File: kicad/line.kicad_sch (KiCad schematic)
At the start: 58 parts, among them J3 AudioJack3_Switch, J4 AudioJack3_Switch, Q2 CSD13380F3, Q3 CSD13380F3, SW12 RotaryEncoder, U12 OPA1637, U13 OPA1637

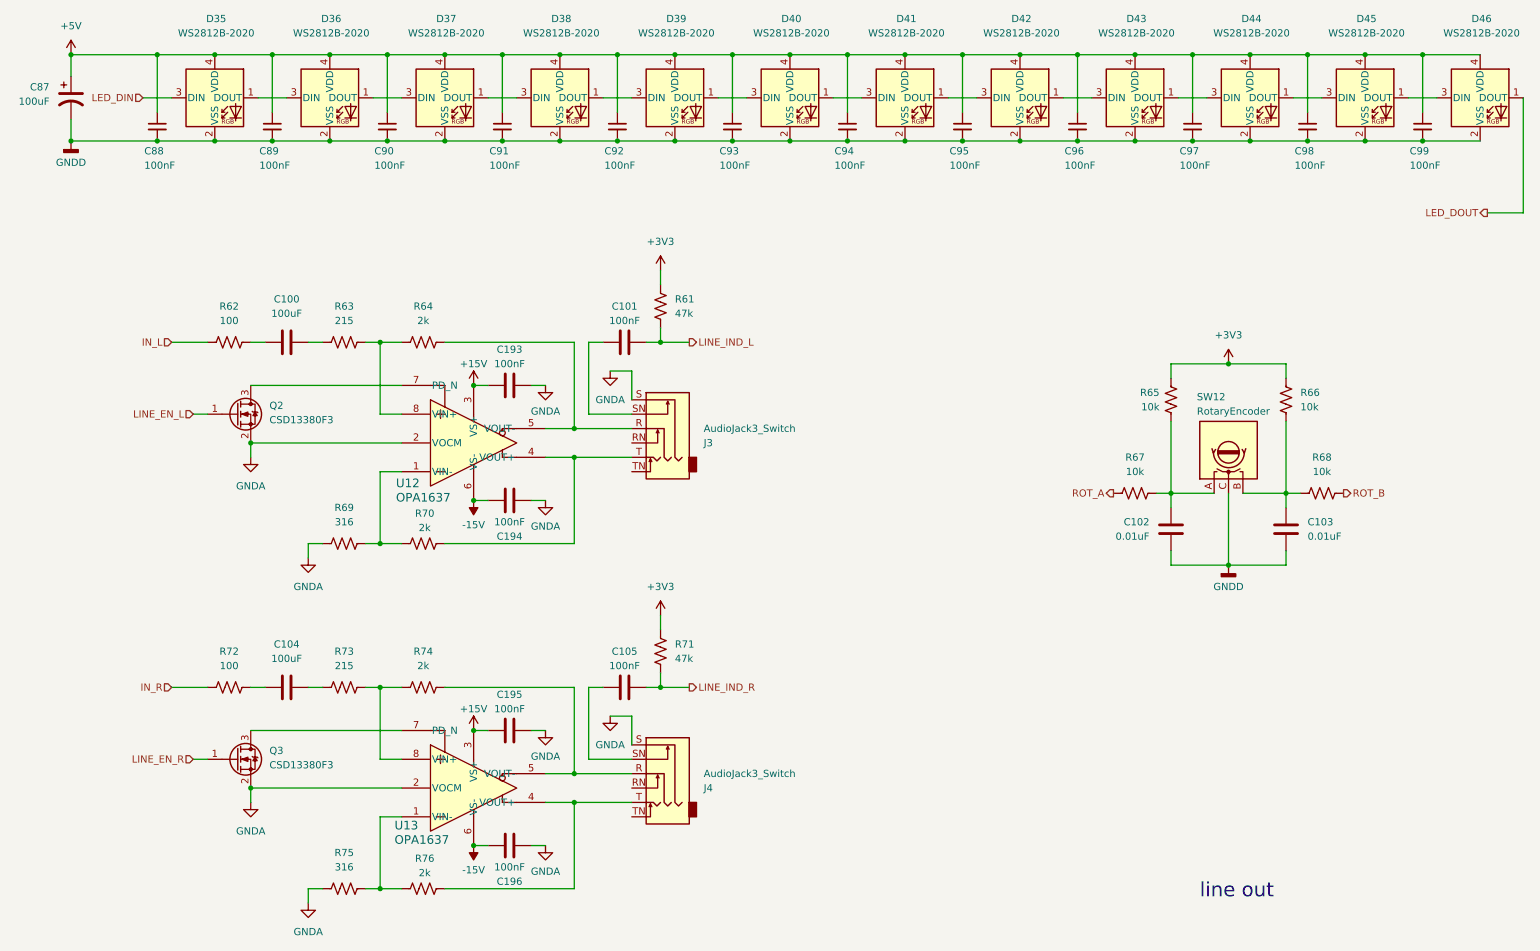
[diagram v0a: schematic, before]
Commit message: output stage impedances
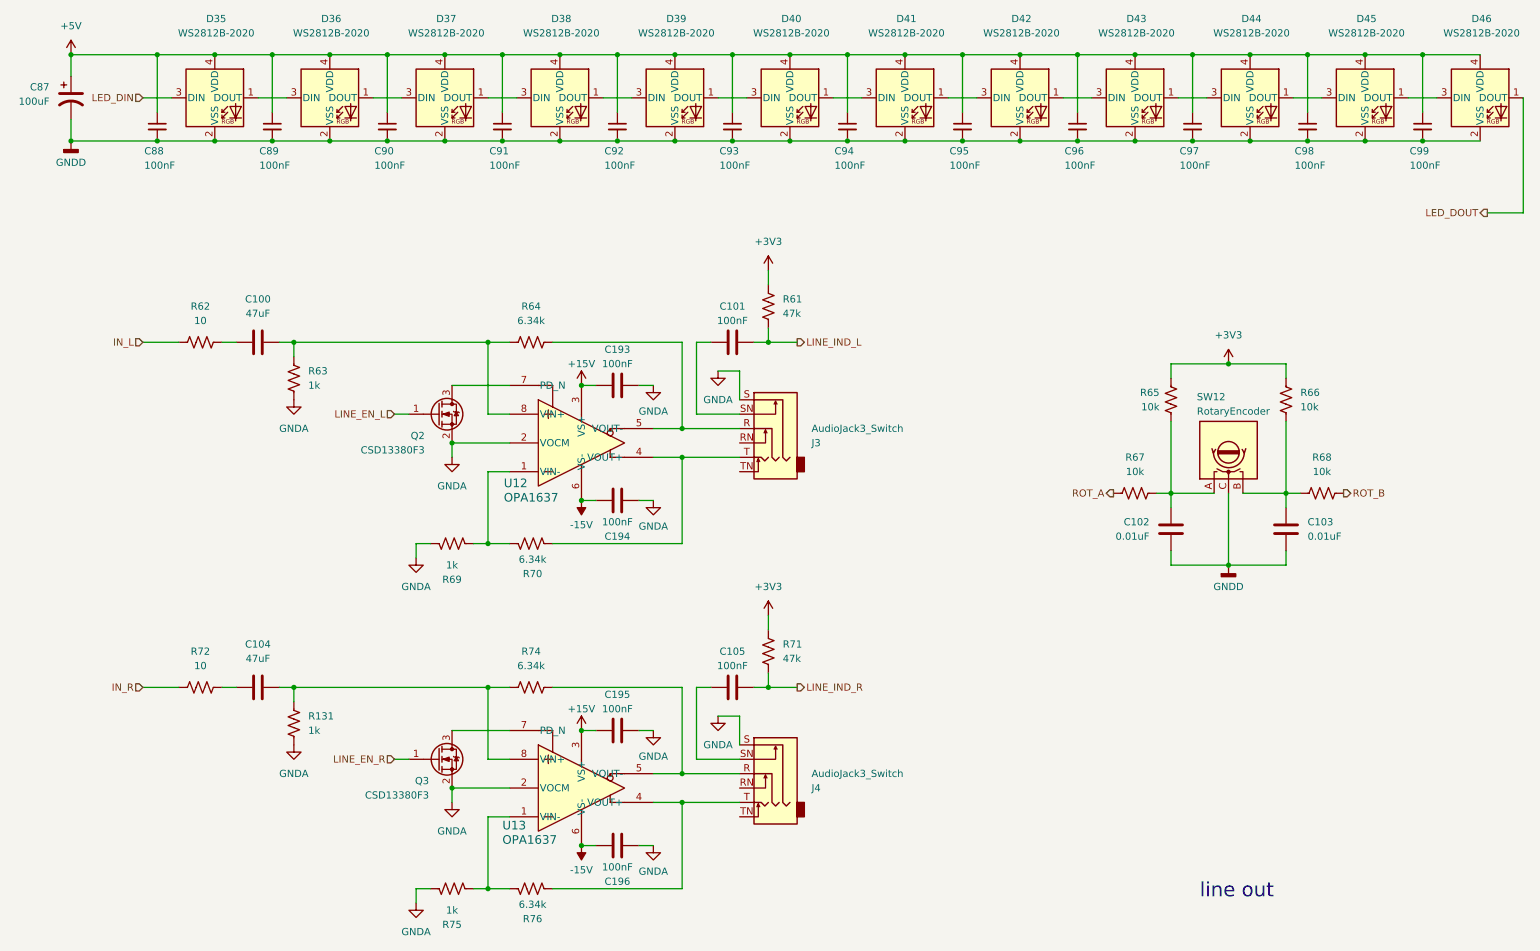
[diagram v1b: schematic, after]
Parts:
- removed R73: 215, symbol Device:R_US
- added R131: 1k, symbol Device:R_US
- C100, C104: value 100uF -> 47uF
- R62, R72: value 100 -> 10
- R63: value 215 -> 1k
- R64, R70, R74, R76: value 2k -> 6.34k
- R69, R75: value 316 -> 1k
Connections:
- net GNDA: now also R63.1, R131.1
- net at R74.1, U13.8 (VIN+): now also C104.2, R131.2
- net at R63.2, R64.1, U12.8 (VIN+): now also C100.2
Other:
- moved on the sheet: C100, C101, C104, C105, C193, C194, C195, C196, J3, J4, Q2, Q3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

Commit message: #16
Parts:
- C102, C103: value 0.01uF -> 10nF
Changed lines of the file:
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@@
 			)
 		)
-		(property "Value" "0.01uF"
+		(property "Value" "10nF"
 			(at 215.9 111.7599 0)
 			(show_name no)
@@
 			)
 		)
-		(property "Value" "0.01uF"
+		(property "Value" "10nF"
 			(at 243.84 111.7599 0)
 			(show_name no)

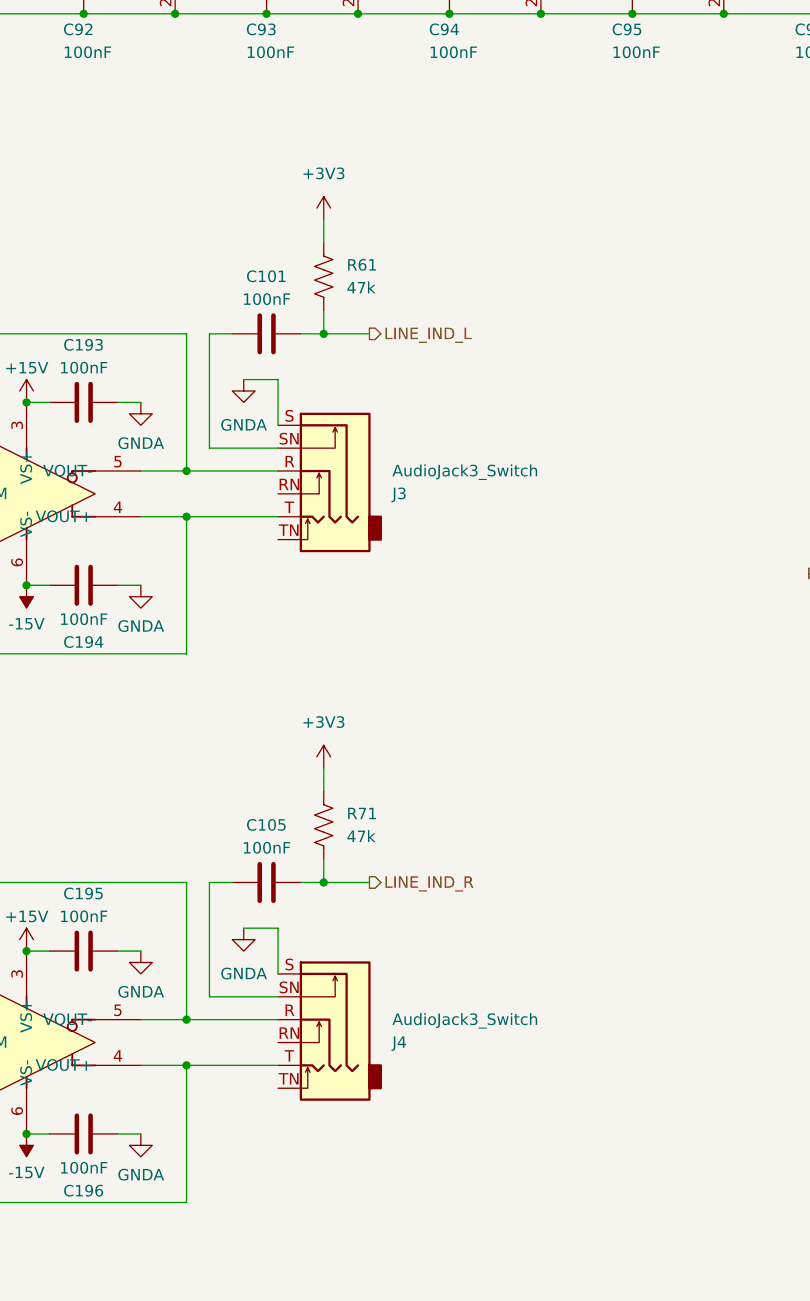
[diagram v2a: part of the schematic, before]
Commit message: push buttons
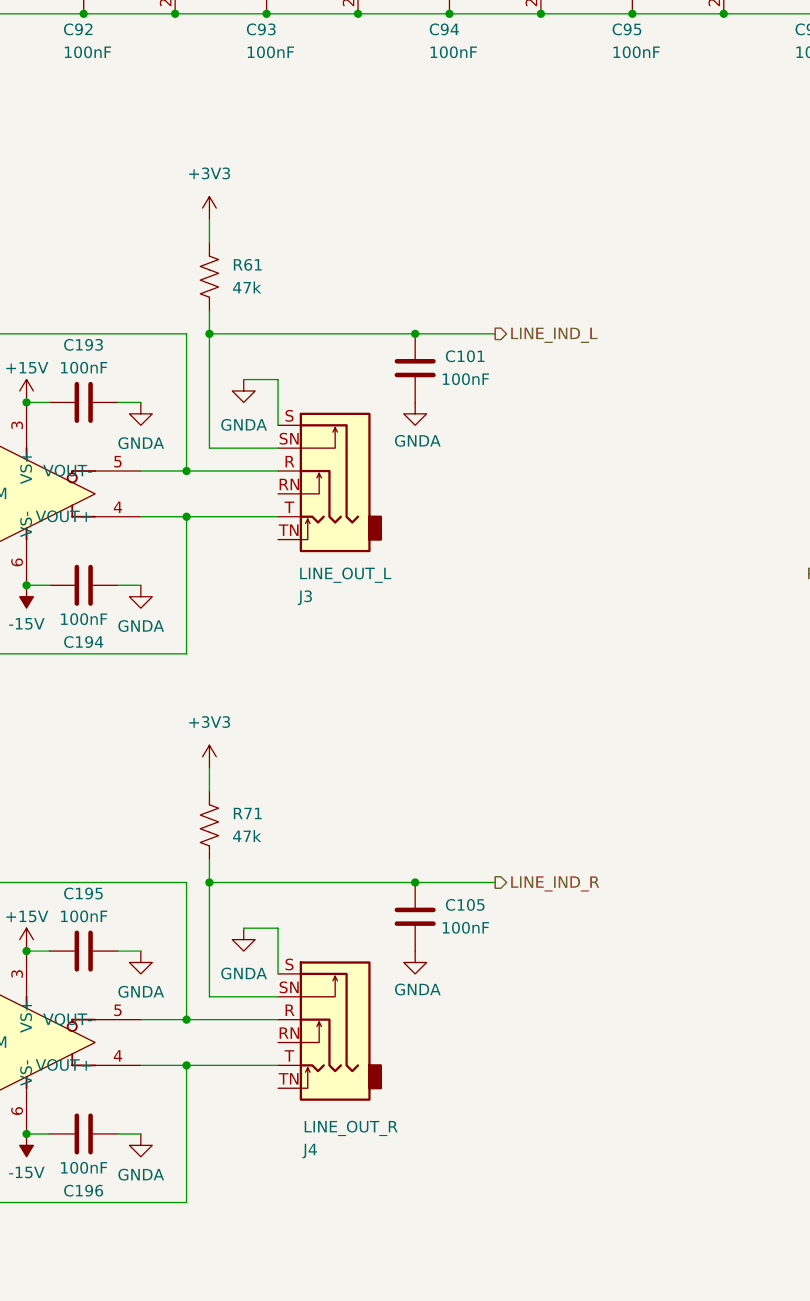
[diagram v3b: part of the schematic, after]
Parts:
- J3: value AudioJack3_Switch -> LINE_OUT_L
- J4: value AudioJack3_Switch -> LINE_OUT_R
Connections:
- net GNDA: now also C101.2, C105.2
- net LINE_IND_L: now also C101.1, J3.SN; no longer C101.2
- net LINE_IND_R: now also C105.1, J4.SN; no longer C105.2
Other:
- moved on the sheet: R61

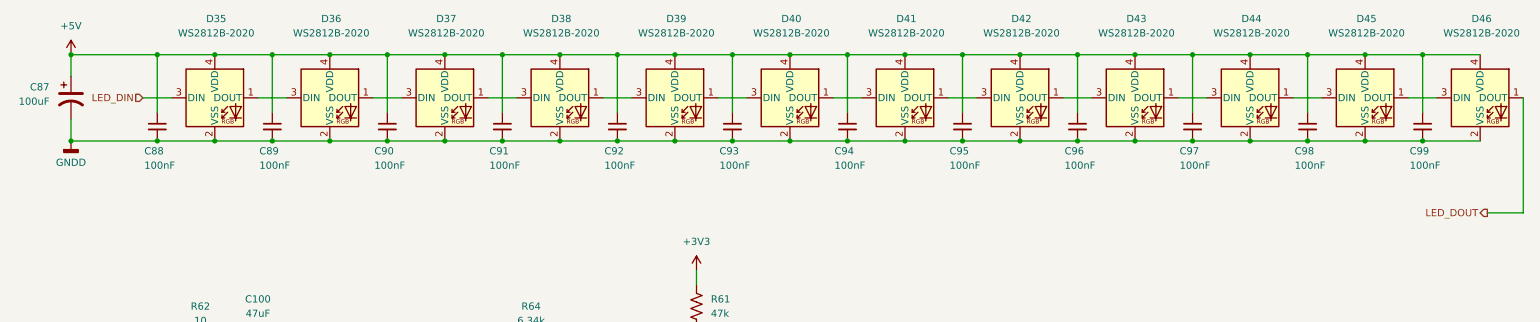
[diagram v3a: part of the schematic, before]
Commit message: reduced ws2812 count
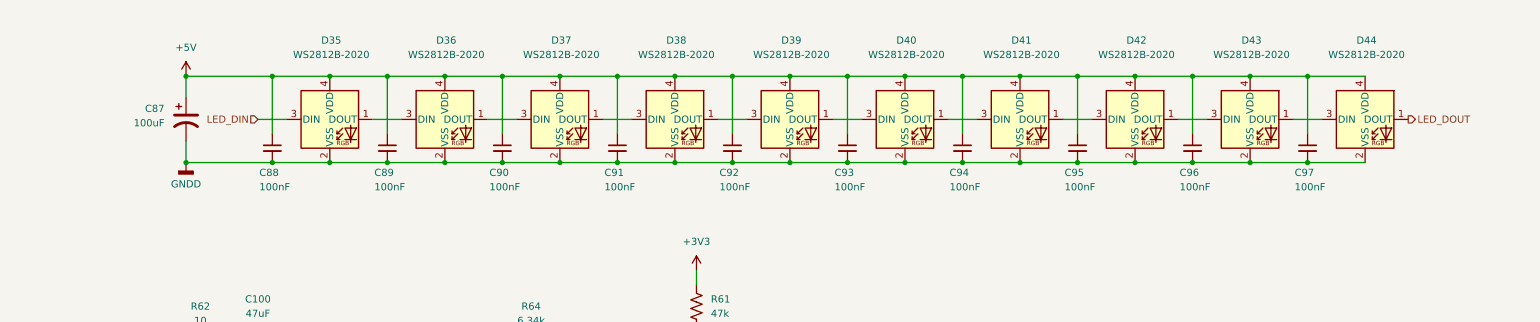
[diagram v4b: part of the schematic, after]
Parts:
- removed C98, C99: 100nF, symbol Device:C_Small
- removed D45, D46: WS2812B-2020, LED_SMD:LED_WS2812B-2020_PLCC4_2.0x2.0mm, symbol LED:WS2812B-2020
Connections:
- net LED_DOUT: now also D44.1 (DOUT)
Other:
- moved on the sheet: C87, C88, C89, C90, C91, C92, C93, C94, C95, C96, C97, D35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

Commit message: added footprints
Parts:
- SW12: footprint (none) -> openmic:PEC11L
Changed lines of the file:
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@@
 			)
 		)
-		(property "Footprint" ""
+		(property "Footprint" "openmic:PEC11L"
 			(at 225.806 100.33 0)
 			(hide yes)

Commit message: footprint selection
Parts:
- removed C100, C104: 47uF, symbol Device:C
- removed C87: 100uF, symbol Device:C_Polarized_US
- added C13: 100uF, Capacitor_SMD:CP_Elec_6.3x5.4, symbol Device:C_Polarized_US
- added C33, C41: 47uF, Capacitor_SMD:CP_Elec_6.3x5.4, symbol Device:C_Polarized_US
- C101, C102, C103, C105, C193, C194, C195, C196, C88, C89, C90, C91, C92, C93, C94, C95, C96, C97: footprint (none) -> Capacitor_SMD:C_0603_1608Metric_Pad1.08x0.95mm_HandSolder
- R131, R61, R62, R63, R64, R65, R66, R67, R68, R69, R70, R71, R72, R74, R75, R76: footprint (none) -> Resistor_SMD:R_0603_1608Metric_Pad0.98x0.95mm_HandSolder
- U12, U13: footprint DGK0008A_N -> (none)
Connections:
- net +5V: now also C13.1
- net GNDD: now also C13.2
- net at R131.2, R74.1, U13.8 (VIN+): now also C41.2
- net at R63.2, R64.1, U12.8 (VIN+): now also C33.2
- net at R72.2: now also C41.1
- net at R62.2: now also C33.1

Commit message: footprints
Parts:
- removed J3: LINE_OUT_L, symbol Connector_Audio:AudioJack3_Switch
- removed J4: LINE_OUT_R, symbol Connector_Audio:AudioJack3_Switch
- added J5: NSJ12HC, Connector_Audio:Jack_6.35mm_Neutrik_NSJ12HC_Horizontal, symbol Connector_Audio:NSJ12HC
- U12, U13: footprint (none) -> Package_SO:VSSOP-8_3x3mm_P0.65mm
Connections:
- net GNDA: now also J5.S1, J5.S2
- net LINE_IND_L: now also J5.SN1
- net LINE_IND_R: now also J5.SN2
- net at R74.2, U13.5 (VOUT-): now also J5.R2
- net at R76.1, U13.4 (VOUT+): now also J5.T2
- net at R70.1, U12.4 (VOUT+): now also J5.T1
- net at R64.2, U12.5 (VOUT-): now also J5.R1
- new net Earth: J5.G
